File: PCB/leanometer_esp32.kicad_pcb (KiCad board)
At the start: 4 copper layers, 91.3 x 63.8 mm, 70 parts, among them J1 Conn_01x07, J2 PROG, J3 VBAT, J4 DM3AT-SF-PEJM5, J5 Conn_01x03, J6 Conn_01x07, J7 Conn_01x03, Q1 BSS138, SW1 SW_Push, SW2 SW_Push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

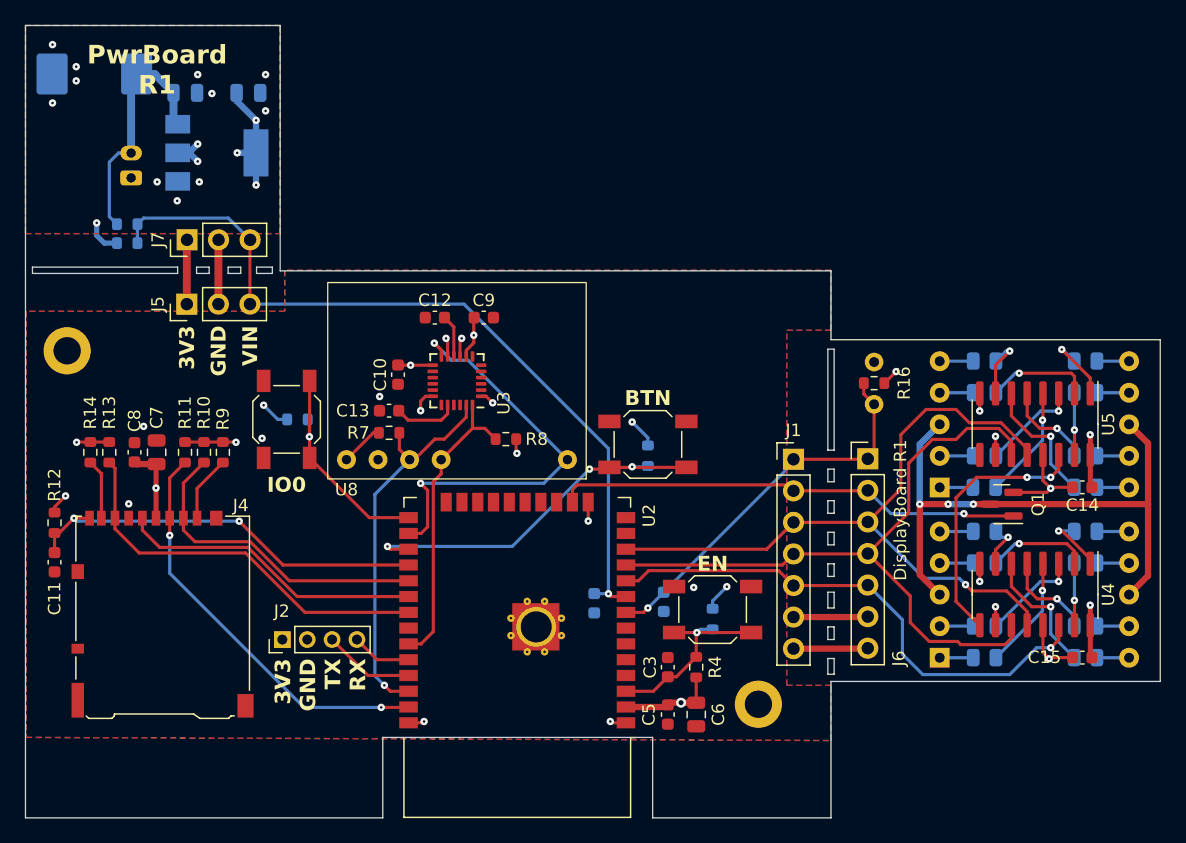
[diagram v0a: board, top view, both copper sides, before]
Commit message: Added RTC circuit
Signed-off-by: theloukou
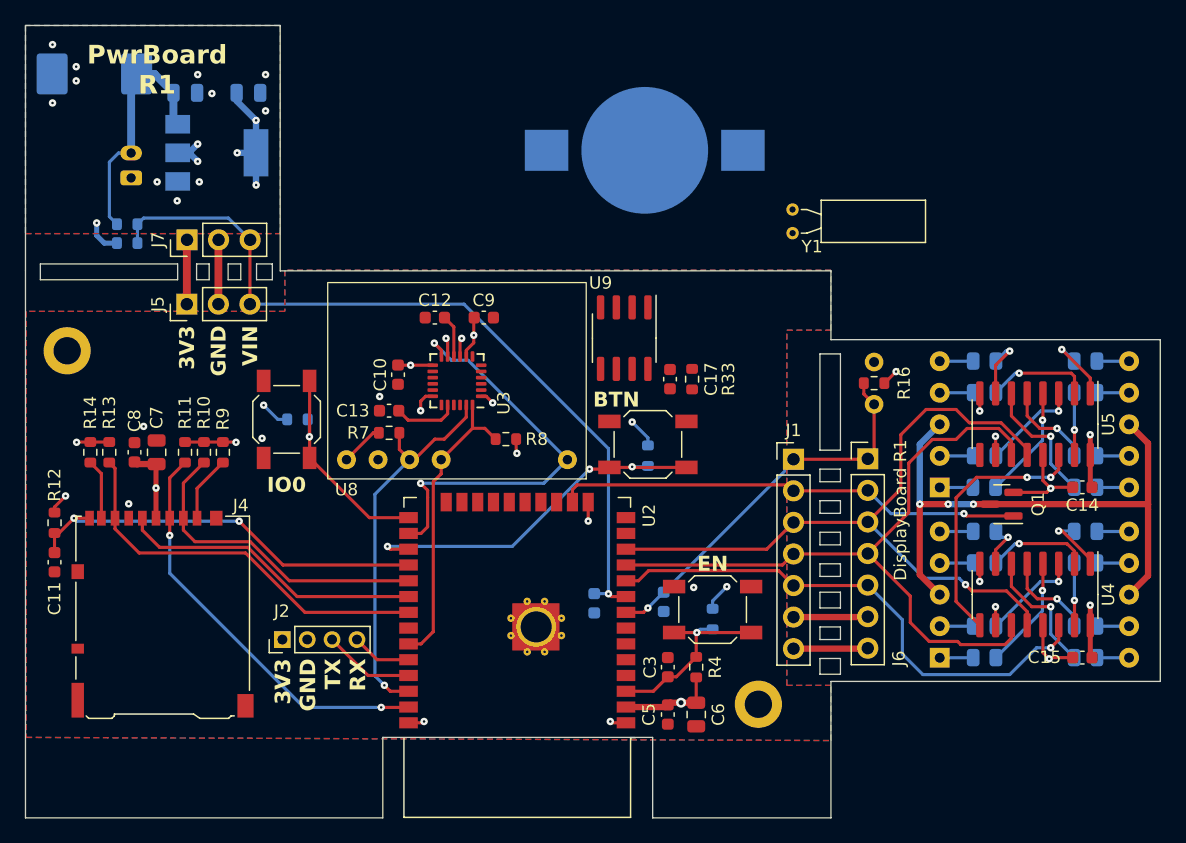
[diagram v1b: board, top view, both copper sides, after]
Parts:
- added BT1: Battery_Cell, Battery:BatteryHolder_Keystone_3000_1x12mm, B.Cu at (150.9, 71.6)
- added C17: 100nF, Capacitor_SMD:C_0603_1608Metric, F.Cu at (152.9, 90.0)
- added R33: 1K, Resistor_SMD:R_0603_1608Metric, F.Cu at (154.7, 90.0)
- added U9: PCF8523, Package_SO:SOIC-8_3.9x4.9mm_P1.27mm, F.Cu at (149.2, 86.7)
- added Y1: 32.768KHz, Crystal:Crystal_C38-LF_D3.0mm_L8.0mm_Horizontal, F.Cu at (162.8, 78.3)
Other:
- outline, holes or cut-outs redrawn

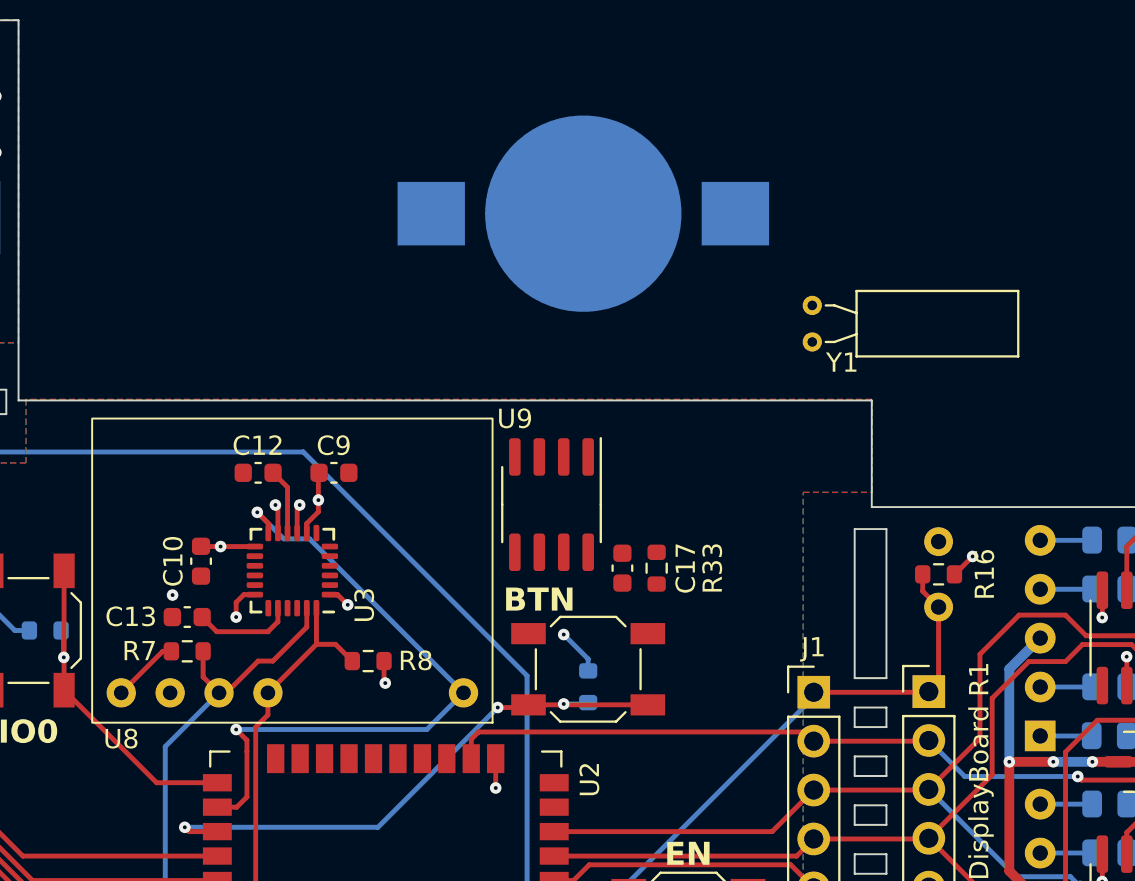
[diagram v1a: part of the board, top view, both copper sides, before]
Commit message: Finalized RTC layout changes
Signed-off-by: theloukou
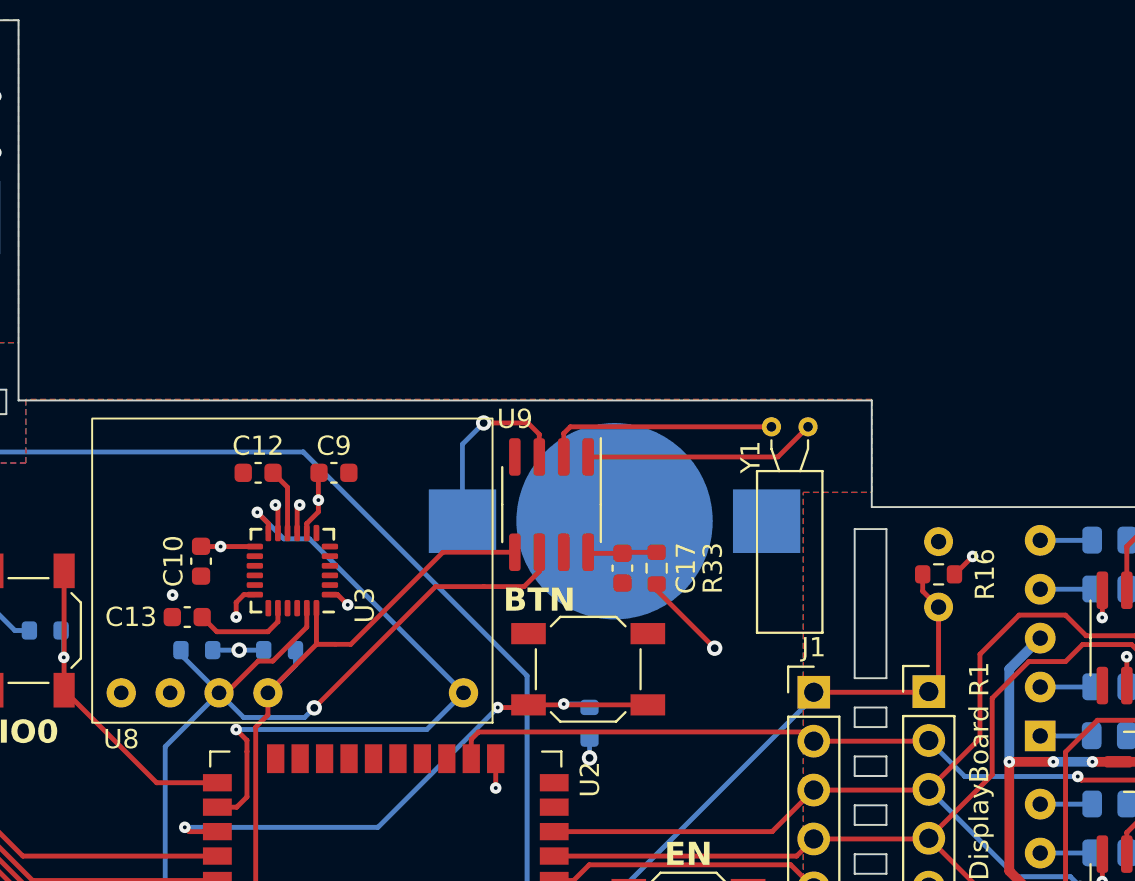
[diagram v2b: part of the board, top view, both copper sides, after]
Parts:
- R7, R8: moved to B.Cu
- moved BT1 16.1 mm to (152.5, 87.6)
- moved Y1 4.89 mm to (160.7, 82.7), turned to 0 degrees
- moved R8 4.64 mm to (135.1, 94.3), turned to 0 degrees
- moved R6 1.90 mm to (151.2, 98.1), turned to 90 degrees
- moved R7 0.50 mm to (130.8, 94.3), turned to 180 degrees
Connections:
- Y1 pad 1: Net-(U9-OSCI) -> Net-(U9-OSCO)
- Y1 pad 2: Net-(U9-OSCO) -> Net-(U9-OSCI)
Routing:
- net /MainBoard/I2C_SCL: track 31.2 -> 53.1 mm, vias 1 -> 2
- net /MainBoard/I2C_SDA: track 24.2 -> 37.1 mm
- net Net-(U9-OSCO): track 0.00 -> 12.2 mm
- net Net-(U9-OSCI): track 0.00 -> 12.1 mm
- net Net-(BT1-+): track 0.00 -> 9.87 mm, vias 0 -> 1
- net Net-(U9-VDD): track 0.00 -> 3.60 mm
- net +3V3: track 76.5 -> 77.6 mm, vias 20 -> 21

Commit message: Minor adjustments on PCB
Signed-off-by: theloukou
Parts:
- moved R8 5.87 mm to (129.4, 92.8)
- moved R7 1.42 mm to (129.4, 94.6), turned to 0 degrees
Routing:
- net /MainBoard/I2C_SDA: track 37.1 -> 40.0 mm
- net +3V3: track 77.6 -> 79.3 mm, vias 21 -> 20
- net GND: vias 29 -> 30
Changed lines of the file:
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@@
   )
   (footprint "Resistor_SMD:R_0603_1608Metric" (layer "B.Cu")
-    (at 130.8 94.3 180)
+    (at 129.413 94.615)
     (descr "Resistor SMD 0603 (1608 Metric), square (rectangular) end terminal, IPC_7351 nominal, (Body size source: IPC-SM-782 page 72, https://www.pcb-3d.com/wordpress/wp-content/uploads/ipc-sm-782a_amendment_1_and_2.pdf), generated with kicad-footprint-generator")
     (tags "resistor")
@@
     (property "ki_keywords" "r resistor")
     (attr smd)
-    (fp_text reference "R7" (at 0 1.4) (layer "B.SilkS")
+    (fp_text reference "R7" (at -2.54 0) (layer "B.SilkS")
         (effects (font (size 1 1) (thickness 0.15)) (justify mirror))
     )
@@
     (fp_line (start 0.8 0.4125) (end 0.8 -0.4125)
       (stroke (width 0.1) (type solid)) (layer "B.Fab"))
-    (pad "1" smd roundrect (at -0.825 0 180) (size 0.8 0.95) (layers "B.Cu" "B.Paste" "B.Mask") (roundrect_rratio 0.25)
+    (pad "1" smd roundrect (at -0.825 0) (size 0.8 0.95) (layers "B.Cu" "B.Paste" "B.Mask") (roundrect_rratio 0.25)
       (net 5 "+3V3") (pintype "passive"))
-    (pad "2" smd roundrect (at 0.825 0 180) (size 0.8 0.95) (layers "B.Cu" "B.Paste" "B.Mask") (roundrect_rratio 0.25)
+    (pad "2" smd roundrect (at 0.825 0) (size 0.8 0.95) (layers "B.Cu" "B.Paste" "B.Mask") (roundrect_rratio 0.25)
       (net 22 "/MainBoard/I2C_SCL") (pintype "passive"))
     (model "${KICAD6_3DMODEL_DIR}/Resistor_SMD.3dshapes/R_0603_1608Metric.wrl"
@@
   )
   (footprint "Resistor_SMD:R_0603_1608Metric" (layer "B.Cu")
-    (at 135.1 94.3)
+    (at 129.413 92.837)
     (descr "Resistor SMD 0603 (1608 Metric), square (rectangular) end terminal, IPC_7351 nominal, (Body size source: IPC-SM-782 page 72, https://www.pcb-3d.com/wordpress/wp-content/uploads/ipc-sm-782a_amendment_1_and_2.pdf), generated with kicad-footprint-generator")
     (tags "resistor")
@@
     (property "ki_keywords" "r resistor")
     (attr smd)
-    (fp_text reference "R8" (at 0 -1.4) (layer "B.SilkS")
+    (fp_text reference "R8" (at -2.54 0) (layer "B.SilkS")
         (effects (font (size 1 1) (thickness 0.15)) (justify mirror))
     )
@@
   (via (at 146.326 101.463) (size 0.6) (drill 0.2) (layers "F.Cu" "B.Cu") (net 1))
   (via (at 136.1427 86.761) (size 0.6) (drill 0.2) (layers "F.Cu" "B.Cu") (net 1))
+  (via (at 151.511 91.059) (size 0.8) (drill 0.4) (layers "F.Cu" "B.Cu") (net 1))
   (via (at 111.633 74.168) (size 0.6) (drill 0.2) (layers "F.Cu" "B.Cu") (free) (net 1))
   (via (at 148.104 117.592) (size 0.6) (drill 0.2) (layers "F.Cu" "B.Cu") (net 1))
@@
   (via (at 120.2055 92.1385) (size 0.6) (drill 0.2) (layers "F.Cu" "B.Cu") (net 5))
   (via (at 186.722 94.514) (size 0.6) (drill 0.2) (layers "F.Cu" "B.Cu") (net 5))
-  (via (at 133 94.3) (size 0.8) (drill 0.4) (layers "F.Cu" "B.Cu") (net 5))
   (via (at 118.075 71.83) (size 0.6) (drill 0.2) (layers "F.Cu" "B.Cu") (free) (net 5))
   (via (at 157.48 106.744) (size 0.6) (drill 0.2) (layers "F.Cu" "B.Cu") (net 5))
@@
   (segment (start 121.3485 93.2815) (end 120.2055 92.1385) (width 0.254) (layer "B.Cu") (net 5))
   (segment (start 156.337 108.522) (end 156.337 107.887) (width 0.254) (layer "B.Cu") (net 5))
+  (segment (start 128.588 92.837) (end 128.588 94.615) (width 0.254) (layer "B.Cu") (net 5))
+  (segment (start 128.588 94.615) (end 126.873 96.33) (width 0.254) (layer "B.Cu") (net 5))
   (segment (start 113.289 71.83) (end 114.19 71.83) (width 0.508) (layer "B.Cu") (net 5))
   (segment (start 114.213 71.83) (end 114.9 72.517) (width 0.508) (layer "B.Cu") (net 5))
@@
   (segment (start 119.589 71.83) (end 118.075 71.83) (width 0.508) (layer "B.Cu") (net 5))
   (segment (start 119.589 71.83) (end 119.589 74.412) (width 0.508) (layer "B.Cu") (net 5))
+  (segment (start 126.873 96.33) (end 126.873 96.52) (width 0.254) (layer "B.Cu") (net 5))
   (segment (start 113.289 71.83) (end 114.213 71.83) (width 0.508) (layer "B.Cu") (net 5))
   (segment (start 122.1005 93.2815) (end 121.3485 93.2815) (width 0.254) (layer "B.Cu") (net 5))
-  (segment (start 131.625 94.3) (end 133 94.3) (width 0.25) (layer "B.Cu") (net 5))
   (segment (start 118.029 67.645) (end 119.599 69.215) (width 0.508) (layer "B.Cu") (net 5))
-  (segment (start 134.275 94.3) (end 133 94.3) (width 0.25) (layer "B.Cu") (net 5))
   (segment (start 119.589 74.412) (end 119.599 74.422) (width 0.508) (layer "B.Cu") (net 5))
   (segment (start 151.2 98.925) (end 151.2 99.9) (width 0.25) (layer "B.Cu") (net 5))
@@
   (via (at 136.9 97.3) (size 0.8) (drill 0.4) (layers "F.Cu" "B.Cu") (net 22))
   (via (at 129.921 114.681) (size 0.6) (drill 0.2) (layers "F.Cu" "B.Cu") (net 22))
+  (segment (start 130.238 94.805) (end 131.953 96.52) (width 0.254) (layer "B.Cu") (net 22))
   (segment (start 136.4 97.8) (end 133.233 97.8) (width 0.25) (layer "B.Cu") (net 22))
-  (segment (start 129.975 94.542) (end 131.953 96.52) (width 0.25) (layer "B.Cu") (net 22))
   (segment (start 136.9 97.3) (end 136.4 97.8) (width 0.25) (layer "B.Cu") (net 22))
   (segment (start 133.233 97.8) (end 131.953 96.52) (width 0.25) (layer "B.Cu") (net 22))
-  (segment (start 129.975 94.3) (end 129.975 94.542) (width 0.25) (layer "B.Cu") (net 22))
   (segment (start 129.159 113.919) (end 129.159 99.314) (width 0.254) (layer "B.Cu") (net 22))
   (segment (start 129.159 99.314) (end 131.953 96.52) (width 0.254) (layer "B.Cu") (net 22))
   (segment (start 129.921 114.681) (end 129.159 113.919) (width 0.254) (layer "B.Cu") (net 22))
+  (segment (start 130.238 94.615) (end 130.238 94.805) (width 0.254) (layer "B.Cu") (net 22))
   (segment (start 147.32 89.216) (end 143.584 89.216) (width 0.25) (layer "F.Cu") (net 23))
   (segment (start 138.8 94) (end 138.006 94) (width 0.25) (layer "F.Cu") (net 23))
@@
   (segment (start 133.858 98.298) (end 134.493 97.663) (width 0.254) (layer "F.Cu") (net 23))
   (segment (start 138.006 94) (end 137.013 94) (width 0.254) (layer "F.Cu") (net 23))
-  (segment (start 135.925 95.088) (end 134.493 96.52) (width 0.25) (layer "B.Cu") (net 23))
-  (segment (start 135.925 94.3) (end 135.925 95.088) (width 0.25) (layer "B.Cu") (net 23))
+  (segment (start 130.81 92.837) (end 134.493 96.52) (width 0.254) (layer "B.Cu") (net 23))
+  (segment (start 130.238 92.837) (end 130.81 92.837) (width 0.254) (layer "B.Cu") (net 23))
   (segment (start 191.38 95.206) (end 191.38 100.102) (width 0.508) (layer "F.Cu") (net 24))
   (segment (start 177.324 100.102) (end 178.6725 100.102) (width 0.508) (layer "F.Cu") (net 24))
